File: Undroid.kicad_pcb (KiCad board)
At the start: 4 copper layers, 95.9 x 108 mm, 39 parts, among them J1 AudioJack2, J2 Conn_01x15

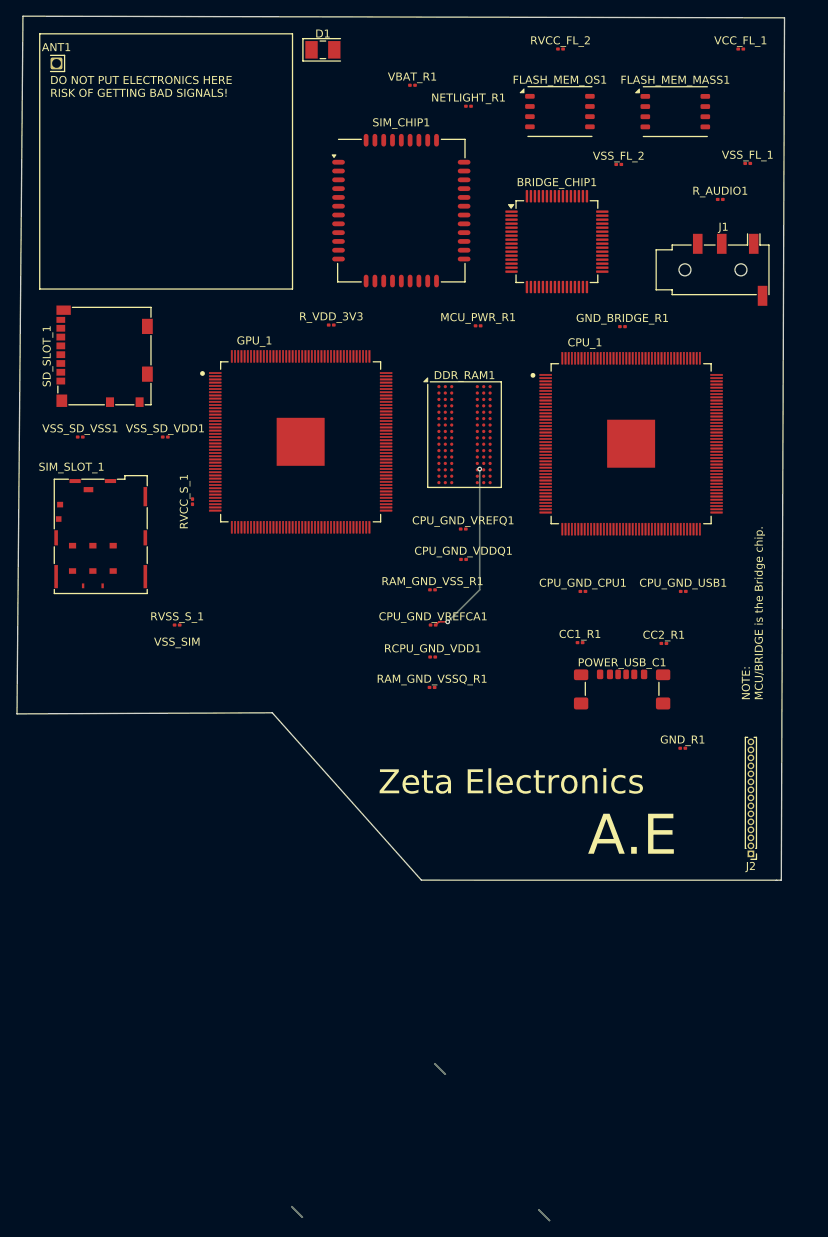
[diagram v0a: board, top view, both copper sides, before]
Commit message: pcb-master: improve schematic and PCB.
Signed-off-by: Amlal EL Mahrouss <amlalelmahrouss@icloud.com>
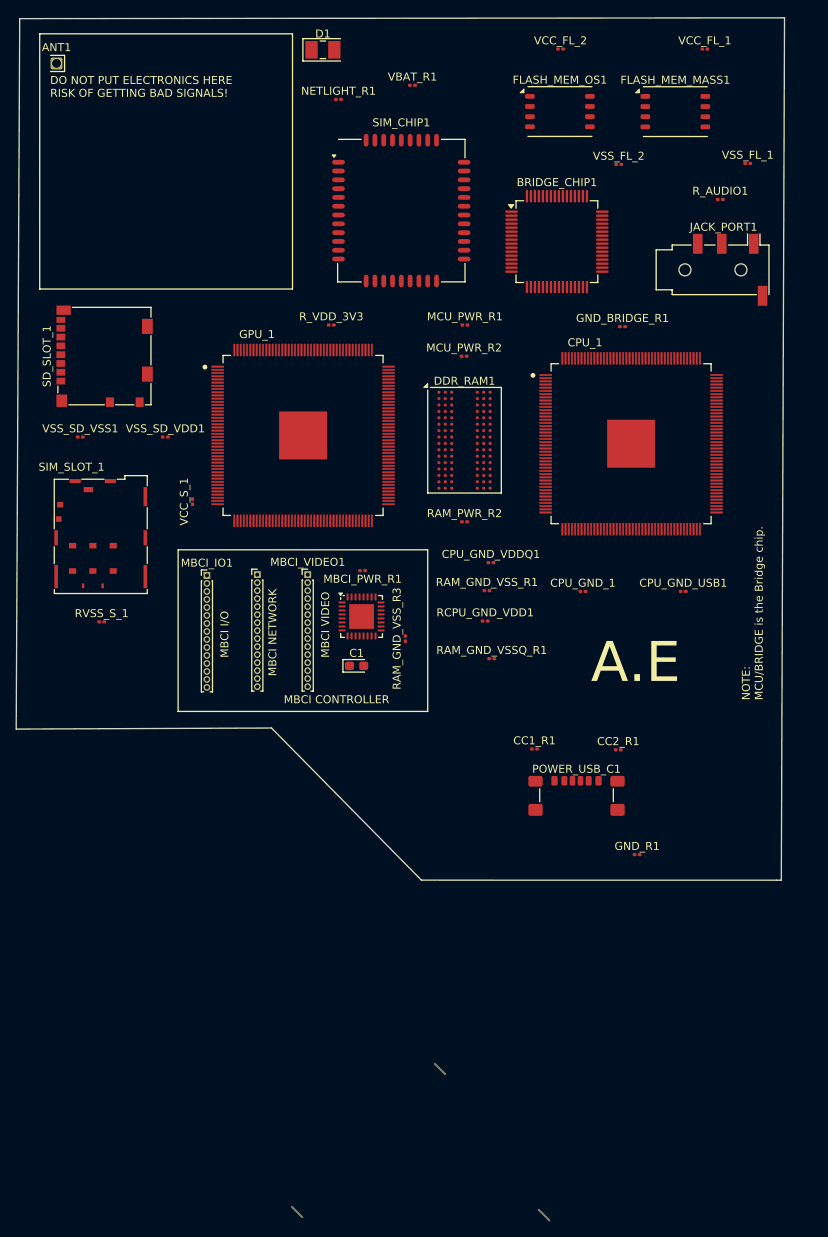
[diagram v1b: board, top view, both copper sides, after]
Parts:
- removed CPU_GND_VREFCA1, CPU_GND_VREFQ1: R, Resistor_SMD:R_0201_0603Metric
- added C1: C_Polarized, Capacitor_Tantalum_SMD:CP_EIA-2012-12_Kemet-R, F.Cu at (129.8, 97.4)
- added MBCI_0: AVR32DB32x-xRXB, Package_DFN_QFN:QFN-32-1EP_5x5mm_P0.5mm_EP3.1x3.1mm, F.Cu at (130.4, 91.2)
- added MBCI_NETWORK1: Conn_01x15, Connector_PinHeader_1.00mm:PinHeader_1x15_P1.00mm_Vertical, F.Cu at (117.4, 86.0)
- added MBCI_PWR_R1: R, Resistor_SMD:R_0201_0603Metric, F.Cu at (130.6, 85.5)
- added MBCI_VIDEO1: Conn_01x15, Connector_PinHeader_1.00mm:PinHeader_1x15_P1.00mm_Vertical, F.Cu at (123.7, 86.0)
- added MCU_PWR_R2: R, Resistor_SMD:R_0201_0603Metric, F.Cu at (143.2, 58.7)
- added RAM_GND_VSS_R3: R, Resistor_SMD:R_0201_0603Metric, F.Cu at (135.9, 94.0)
- added RAM_PWR_R2: R, Resistor_SMD:R_0201_0603Metric, F.Cu at (143.3, 79.4)
- moved MBCI_IO1 76.4 mm to (111.1, 86.1), turned to 0 degrees
- moved NETLIGHT_R1 16.3 mm to (127.5, 26.6)
- moved CC2_R1 14.5 mm to (162.5, 107.9)
- moved CC1_R1 14.5 mm to (152.0, 107.8)
- moved GND_R1 14.5 mm to (164.9, 121.0)
- moved POWER_USB_C1 14.5 mm to (157.3, 114.8)
- moved RVSS_S_1 9.44 mm to (97.9, 91.9)
- moved RAM_GND_VSSQ_R1 8.28 mm to (146.7, 96.5)
- moved RCPU_GND_VDD1 7.96 mm to (145.9, 91.8)
- moved RAM_GND_VSS_R1 6.80 mm to (146.1, 88.0)
- moved VCC_FL_1 4.49 mm to (173.3, 20.3)
- moved CPU_GND_VDDQ1 3.44 mm to (146.6, 84.5)
- moved MCU_PWR_R1 1.66 mm to (143.3, 54.8)
- moved GPU_1 0.86 mm to (123.1, 68.6)
- moved DDR_RAM1 0.70 mm to (143.3, 69.2)
- renumbered CPU_GND_CPU1 to CPU_GND_1, J1 to JACK_PORT1, J2 to MBCI_IO1, RVCC_FL_2 to VCC_FL_2, RVCC_S_1 to VCC_S_1
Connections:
- CPU_1 pad 100: +3.3V -> CPU_PWR
- CPU_1 pad 109: +3.3V -> unconnected-(CPU_1A-VDD_INT-Pad109)_1
- CPU_1 pad 11: +3.3V -> unconnected-(CPU_1A-VDD_CPU-Pad11)
- CPU_1 pad 142: +3.3V -> CPU_PWR
- CPU_1 pad 149: +3.3V -> unconnected-(CPU_1A-VDD_INT-Pad109)_3
- CPU_1 pad 156: +3.3V -> unconnected-(CPU_1A-VDD_CPU-Pad11)_1
- CPU_1 pad 16: +3.3V -> unconnected-(CPU_1A-VDD_CPU-Pad11)_0
- CPU_1 pad 163: +3.3V -> CPU_PWR
- CPU_1 pad 164: +3.3V -> unconnected-(CPU_1A-VDD_CPU-Pad11)_4
- CPU_1 pad 169: +3.3V -> unconnected-(CPU_1A-VDD_CPU-Pad11)_3
- CPU_1 pad 173: +3.3V -> unconnected-(CPU_1A-VDD_CPU-Pad11)_5
- CPU_1 pad 18: Net-(CPU_1A-SVREF) -> unconnected-(CPU_1A-SVREF-Pad18)
- CPU_1 pad 23: +3.3V -> DRAM_PWR
- CPU_1 pad 30: +3.3V -> DRAM_PWR
- CPU_1 pad 35: +3.3V -> unconnected-(CPU_1A-VDD_INT-Pad109)_0
- CPU_1 pad 4: +3.3V -> unconnected-(CPU_1A-VDD_CPU-Pad11)_2
- CPU_1 pad 43: +3.3V -> DRAM_PWR
- CPU_1 pad 5: +3.3V -> CPU_PWR
- CPU_1 pad 53: +3.3V -> DRAM_PWR
- CPU_1 pad 62: +3.3V -> DRAM_PWR
- CPU_1 pad 73: +3.3V -> unconnected-(CPU_1A-VDD_INT-Pad109)
- CPU_1 pad 76: Net-(CPU_1A-SVREF) -> unconnected-(CPU_1A-V33_HP-Pad76)
- CPU_1 pad 81: +3.3V -> unconnected-(CPU_1A-AVCC-Pad81)
- CPU_1 pad 85: Net-(CPU_1A-SVREF) -> unconnected-(CPU_1A-VMIC-Pad85)
- CPU_1 pad 9: +3.3V -> unconnected-(CPU_1A-VDD_CPU-Pad11)_6
- CPU_1 pad 97: Net-(CPU_1A-SVREF) -> unconnected-(CPU_1A-V33_USB-Pad97)
- CPU_1 pad 98: +3.3V -> unconnected-(CPU_1A-VDD_INT-Pad109)_2
- DDR_RAM1 pad A1: Net-(CPU_GND_VDDQ1-Pad2) -> unconnected-(DDR_RAM1-VDDQ-PadA1)
- DDR_RAM1 pad A8: Net-(CPU_GND_VDDQ1-Pad2) -> unconnected-(DDR_RAM1-VDDQ-PadA1)_2
- DDR_RAM1 pad C1: Net-(CPU_GND_VDDQ1-Pad2) -> unconnected-(DDR_RAM1-VDDQ-PadA1)_3
- DDR_RAM1 pad C9: Net-(CPU_GND_VDDQ1-Pad2) -> unconnected-(DDR_RAM1-VDDQ-PadA1)_6
- DDR_RAM1 pad D2: Net-(CPU_GND_VDDQ1-Pad2) -> unconnected-(DDR_RAM1-VDDQ-PadA1)_5
- DDR_RAM1 pad E9: Net-(CPU_GND_VDDQ1-Pad2) -> unconnected-(DDR_RAM1-VDDQ-PadA1)_0
- DDR_RAM1 pad F1: Net-(CPU_GND_VDDQ1-Pad2) -> unconnected-(DDR_RAM1-VDDQ-PadA1)_7
- DDR_RAM1 pad H1: Net-(DDR_RAM1-VREFDQ) -> unconnected-(DDR_RAM1-VREFDQ-PadH1)
- DDR_RAM1 pad H2: Net-(CPU_GND_VDDQ1-Pad2) -> unconnected-(DDR_RAM1-VDDQ-PadA1)_4
- DDR_RAM1 pad H9: Net-(CPU_GND_VDDQ1-Pad2) -> unconnected-(DDR_RAM1-VDDQ-PadA1)_1
- DDR_RAM1 pad M8: Net-(DDR_RAM1-VREFCA) -> unconnected-(DDR_RAM1-VREFCA-PadM8)
- MBCI_IO1 pad 11: unconnected-(J2-Pin_11-Pad11) -> CLK
- MBCI_IO1 pad 15: unconnected-(J2-Pin_15-Pad15) -> GND
- MBCI_IO1 pad 5: unconnected-(J2-Pin_5-Pad5) -> UBOOT_MBCI
- MBCI_IO1 pad 8: unconnected-(J2-Pin_8-Pad8) -> 3.3V
- MCU_PWR_R1 pad 2: +3.3V -> VBUS_USBC
- R_VDD_3V3 pad 1: +3.3V -> VBUS_USBC
- VBAT_R1 pad 1: +3.3V -> VBUS_USBC
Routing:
- net Net-(DDR_RAM1-VREFCA): track 22.4 -> 0.00 mm, vias 2 -> 0
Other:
- board size 95.9 x 108 mm -> 96 x 107.8 mm
- board text added: "MBCI CONTROLLER"
- board text added: "MBCI I/O"
- board text added: "MBCI NETWORK"
- board text added: "MBCI VIDEO"
- board text removed: "VSS_SIM"
- board text removed: "Zeta Electronics"

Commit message: pcb-master: update PCB layout.
Signed-off-by: Amlal El Mahrouss <amlal.elmahrouss@icloud.com>
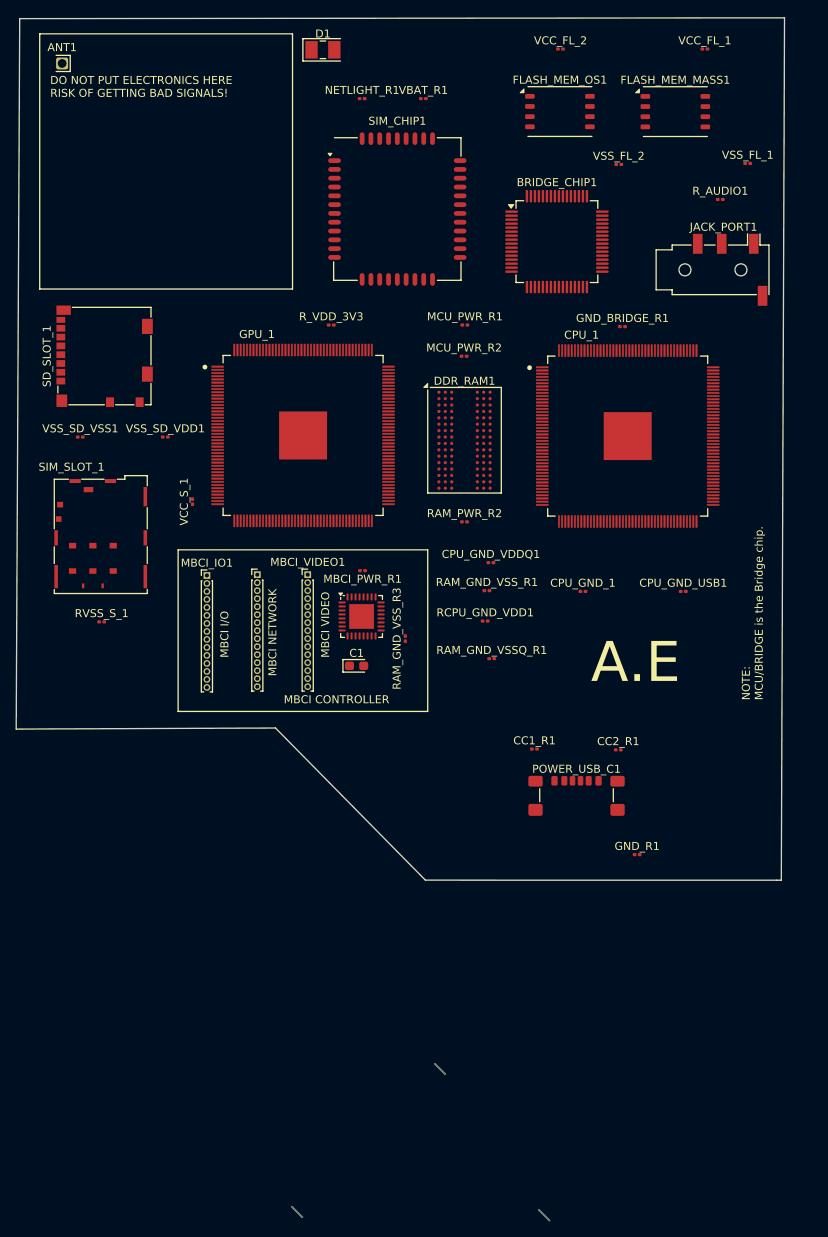
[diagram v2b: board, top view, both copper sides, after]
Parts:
- moved NETLIGHT_R1 2.96 mm to (130.5, 26.5)
- moved VBAT_R1 2.15 mm to (138.2, 26.5)
- moved CPU_1 1.05 mm to (163.7, 68.7)
- moved ANT1 0.70 mm to (93.0, 22.1)
- moved SIM_CHIP1 0.54 mm to (134.9, 40.3)
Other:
- outline, holes or cut-outs redrawn

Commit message: board: major improvements.
Signed-off-by: Amlal EL Mahrouss <amlalelmahrouss@icloud.com>
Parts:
- removed CPU_GND_USB1, CPU_GND_VDDQ1, RCPU_GND_VDD1: R, Resistor_SMD:R_0201_0603Metric
- removed GPU_1: Allwinner-A13, Allwinner:QFP40P2200X2200X160-177N
- moved JACK_PORT1 107.2 mm to (176.5, 155.1), turned to 180 degrees
- moved R_AUDIO1 106.5 mm to (165.0, 145.1), turned to 90 degrees
- moved RVSS_S_1 97.6 mm to (175.1, 32.1), turned to 90 degrees
- moved ANT1 91.0 mm to (183.0, 35.6), turned to 90 degrees
- moved SIM_SLOT_1 88.9 mm to (174.9, 40.5), turned to 0 degrees
- moved VCC_S_1 76.6 mm to (172.7, 33.9), turned to 0 degrees
- moved VBAT_R1 72.9 mm to (180.2, 86.1)
- moved SIM_CHIP1 70.3 mm to (176.1, 97.3)
- moved MBCI_IO1 67.0 mm to (164.4, 126.7)
- moved MBCI_NETWORK1 66.4 mm to (169.9, 126.7)
- moved MBCI_VIDEO1 66.0 mm to (175.6, 126.8)
- moved R_VDD_3V3 60.2 mm to (166.0, 100.4), turned to 90 degrees
- moved VSS_SD_VSS1 55.9 mm to (141.3, 37.1), turned to 90 degrees
- moved DDR_RAM1 55.9 mm to (136.5, 124.7), turned to 90 degrees
- moved C1 53.0 mm to (178.3, 118.7), turned to -90 degrees
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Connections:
- BRIDGE_CHIP1 pad 2: A14 -> RAM_BA2
- BRIDGE_CHIP1 pad 20: A12/BC_N -> RAM_BA0
- BRIDGE_CHIP1 pad 21: A13 -> RAM_BA1
- BRIDGE_CHIP1 pad 37: PWR_TST -> unconnected-(BRIDGE_CHIP1-TST-Pad37)
- BRIDGE_CHIP1 pad 46: TX2 -> unconnected-(BRIDGE_CHIP1-PB4-Pad46)
- BRIDGE_CHIP1 pad 47: RX2 -> unconnected-(BRIDGE_CHIP1-PB5-Pad47)
- MBCI_0 pad 11: unconnected-(MBCI_0-PD1-Pad11) -> A11
- MBCI_0 pad 12: unconnected-(MBCI_0-PD2-Pad12) -> A12/BC_N
- MBCI_0 pad 13: unconnected-(MBCI_0-PD3-Pad13) -> A13
- MBCI_0 pad 14: unconnected-(MBCI_0-PD4-Pad14) -> A14
- MBCI_0 pad 15: unconnected-(MBCI_0-PD5-Pad15) -> RAM_BA2
- MBCI_0 pad 16: unconnected-(MBCI_0-PD6-Pad16) -> RAM_BA1
- MBCI_0 pad 17: unconnected-(MBCI_0-VREFA/PD7-Pad17) -> RAM_BA0
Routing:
- added copper zone on B.Cu, net GND
- added copper zone on F.Cu, net GND
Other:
- board size 96 x 107.8 mm -> 60.9 x 132 mm
- copper layers 4 -> 2
- board text added: "BRIDGE"
- board text added: "CPU"
- board text added: "EU-B"
- board text added: "MBCI"
- board text added: "ZETA-001"
- board text removed: "A.E"
- board text removed: "DO NOT PUT ELECTRONICS HERE RISK OF GETTING BAD SIGNALS!"
- board text removed: "MBCI CONTROLLER"
- board text removed: "MBCI I/O"
- board text removed: "MBCI NETWORK"
- board text removed: "MBCI VIDEO"
- board text removed: "NOTE: MCU/BRIDGE is the Bridge chip."

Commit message: Finishing routing.
Signed-off-by: Amlal EL Mahrouss <amlalelmahrouss@icloud.com>
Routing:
- net VBUS_USBC: track 0.00 -> 219.2 mm, vias 0 -> 3
- net RAM_BA2: track 0.00 -> 205.6 mm, vias 0 -> 10
- net RTC_OUT: track 0.00 -> 168.4 mm, vias 0 -> 5
- net A11: track 0.00 -> 133.6 mm, vias 0 -> 10
- net A1: track 0.00 -> 126.5 mm, vias 0 -> 15
- net RAM_BA1: track 0.00 -> 121.2 mm, vias 0 -> 11
- net RESET: track 0.00 -> 111.3 mm, vias 0 -> 5
- net A2: track 0.00 -> 111.2 mm, vias 0 -> 8
- net RTS1: track 0.00 -> 100.4 mm, vias 0 -> 4
- net A3: track 0.00 -> 89.4 mm, vias 0 -> 8
- net GSM_IO: track 0.00 -> 87.1 mm, vias 0 -> 3
- net RAM_BA0: track 0.00 -> 84.2 mm, vias 0 -> 3
- net SD_DAT2: track 0.00 -> 78.6 mm, vias 0 -> 2
- net DQ13: track 0.00 -> 78.1 mm, vias 0 -> 2
- net CPU_PWR: track 0.00 -> 76.8 mm, vias 0 -> 2
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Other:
- board size 60.9 x 132 mm -> 61.7 x 133.2 mm
- board text added: "A.E"
- board text added: "OS/BOOT"
- board text added: "STORE"
- board text removed: "EU-B"

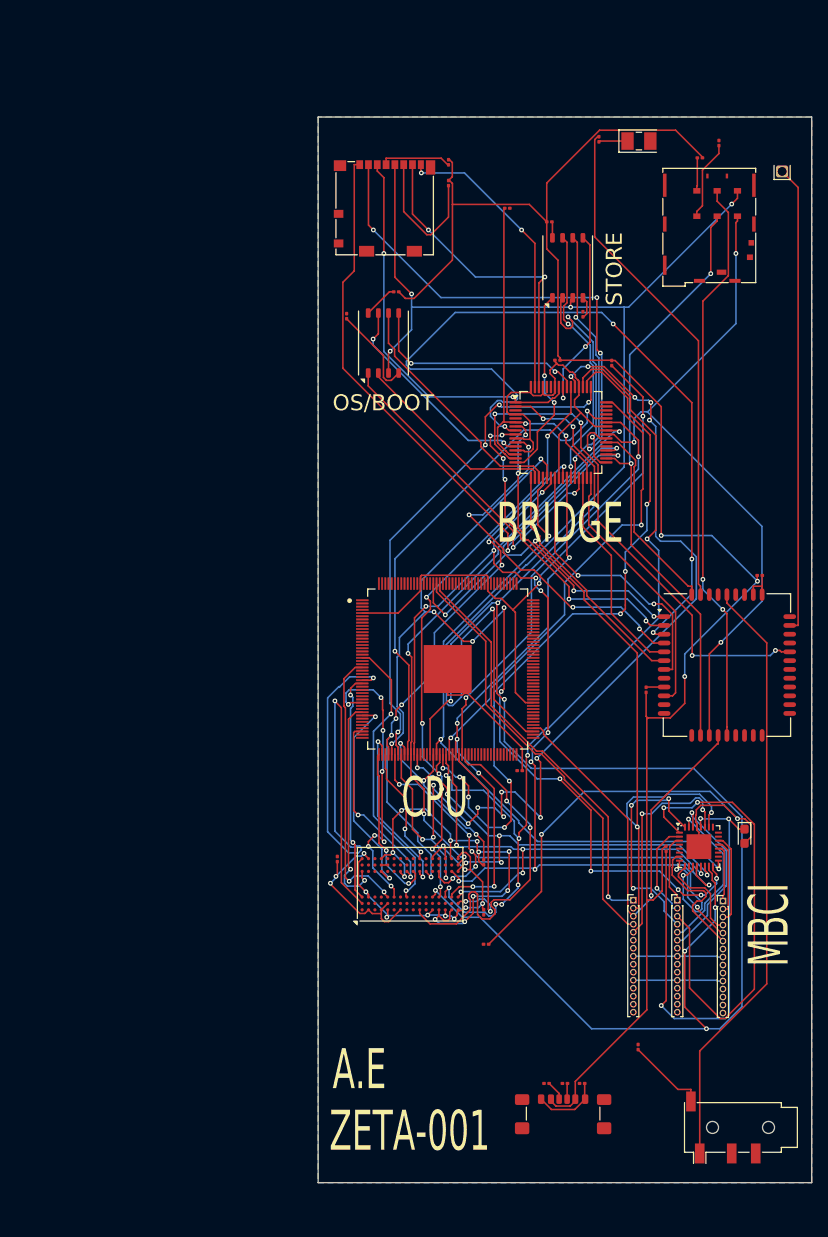
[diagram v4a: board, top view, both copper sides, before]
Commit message: pcb-master: Start of step 2: Finish and improve routing of motherboard.
Signed-off-by: Amlal EL Mahrouss <amlalelmahrouss@icloud.com>
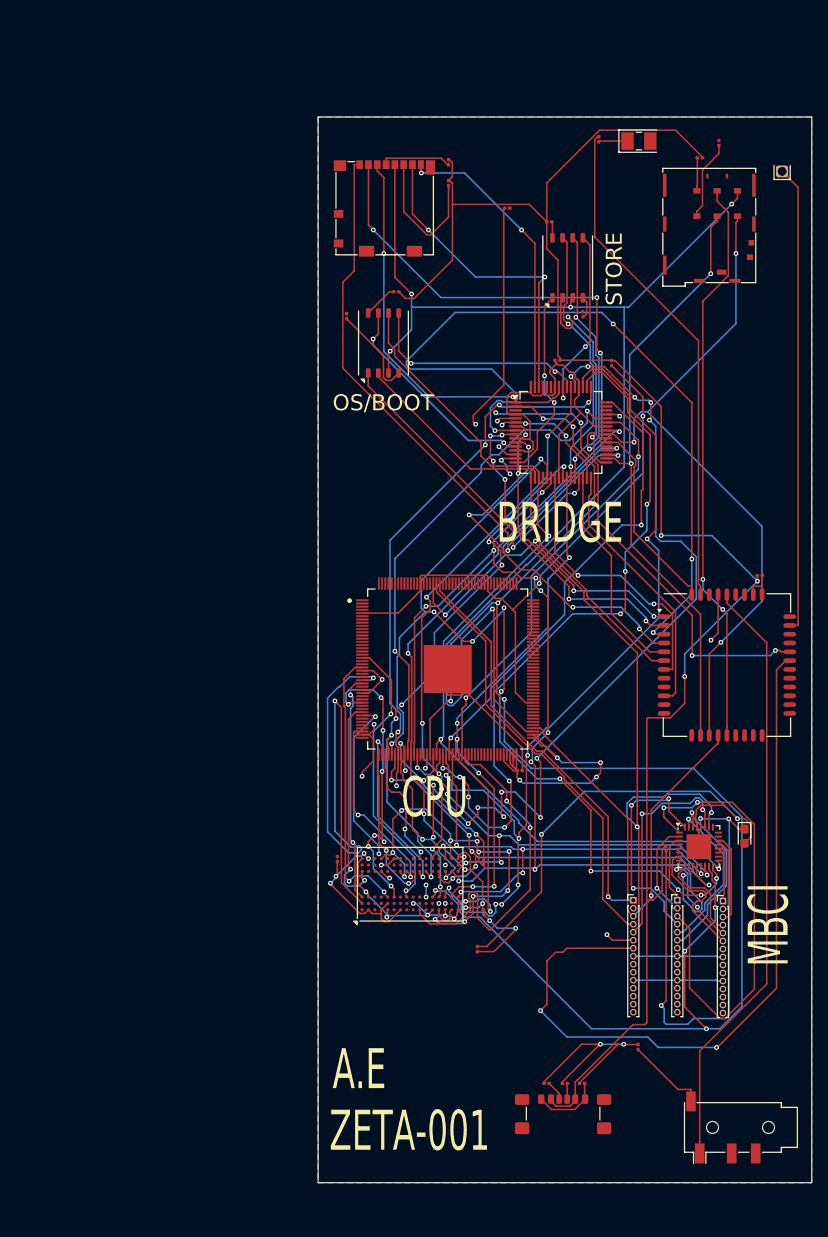
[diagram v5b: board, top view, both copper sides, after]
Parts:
- removed R_VDD_3V3: R, Resistor_SMD:R_0201_0603Metric
- moved RAM_GND_VSS_R3 1.25 mm to (144.9, 132.8), turned to 90 degrees
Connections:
- MBCI_IO1 pad 6: unconnected-(MBCI_IO1-Pin_6-Pad6) -> GSM_PWR_N
- MBCI_IO1 pad 7: unconnected-(MBCI_IO1-Pin_7-Pad7) -> GSM_RST_N
- SIM_CHIP1 pad 28: unconnected-(SIM_CHIP1-~{RESET}-Pad28) -> GSM_RST_N
- SIM_CHIP1 pad 39: GND -> GSM_PWR_N
- SIM_CHIP1 pad 9: Net-(SIM_CHIP1-VDD_3V3) -> unconnected-(SIM_CHIP1-VDD_3V3-Pad9)
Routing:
- net GND: track 0.00 -> 96.6 mm, vias 0 -> 10
- net GSM_RST_N: track 0.00 -> 94.4 mm, vias 0 -> 2
- net GSM_PWR_N: track 0.00 -> 57.9 mm, vias 0 -> 2
- net DRAM_PWR: track 24.6 -> 54.7 mm, vias 3 -> 7
- net A5: track 57.8 -> 83.0 mm, vias 2 -> 3
- net RAM_WE_N: track 0.00 -> 19.0 mm, vias 0 -> 3
- net A4: track 63.9 -> 81.9 mm, vias 4 -> 6
- net A3: track 89.4 -> 103.9 mm, vias 8 -> 9
- net GSM_GPIO_1: track 65.7 -> 74.2 mm, vias 4 -> 6
- net Net-(BRIDGE_CHIP1-GND-Pad14): track 47.4 -> 55.3 mm, vias 2 -> 5
- net Net-(DDR_RAM1-VSSQ-PadB1): track 23.2 -> 27.1 mm, vias 3 -> 5
- net Net-(DDR_RAM1-VSS-PadA9): track 43.9 -> 46.3 mm, vias 9 -> 10
- net VBUS_USBC: track 219.2 -> 216.9 mm
- net Net-(SIM_CHIP1-VDD_3V3): track 2.26 -> 0.00 mm
- net DQ08: track 26.3 -> 28.2 mm, vias 2 -> 3
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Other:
- copper layers 2 -> 4
